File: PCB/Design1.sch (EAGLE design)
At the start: 38 parts, among them J1 FTDI_DEVICE, U1 ATMEGA2560AU

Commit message: meh
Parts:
- added R10: 1MΩ, SparkFun-Resistors:RESISTOR1206
- added Y1: 16MHZ, SparkFun-FreqCtrl:RESONATOR16MHZ
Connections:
- net N$8 renamed VIN_RECTIFIED
- new net XTAL1: R10.1, U1.XTAL1, Y1.3
- new net XTAL2: R10.2, U1.XTAL2, Y1.1
- net GND: now also Y1.2
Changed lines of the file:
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@@
 <part name="U3" library="SparkFun-PowerIC" deviceset="V_REG_LM1117" device="SOT223"/>
 <part name="C7" library="SparkFun-Capacitors" deviceset="CAP_POL" device="PTH1" value="470uF"/>
+<part name="Y1" library="SparkFun-FreqCtrl" deviceset="RESONATOR" device="16MHZ" value="16MHZ"/>
+<part name="R10" library="SparkFun-Resistors" deviceset="RESISTOR" device="1206" value="1MΩ"/>
+<part name="GND8" library="SparkFun-Aesthetics" deviceset="GND" device=""/>
 </parts>
 <sheets>
@@
 <instance part="POWER" gate="G$1" x="5.08" y="33.02"/>
 <instance part="SERIAL" gate="G$1" x="256.54" y="73.66"/>
-<instance part="SUPPLY1" gate="G$1" x="60.96" y="205.74"/>
+<instance part="SUPPLY1" gate="G$1" x="60.96" y="200.66"/>
 <instance part="SUPPLY3" gate="G$1" x="238.76" y="25.4"/>
 <instance part="SUPPLY5" gate="G$1" x="111.76" y="43.18"/>
@@
 <instance part="U3" gate="G$1" x="63.5" y="20.32" rot="MR180"/>
 <instance part="C7" gate="G$1" x="81.28" y="35.56"/>
+<instance part="Y1" gate="G$1" x="53.34" y="210.82" rot="R270"/>
+<instance part="R10" gate="G$1" x="33.02" y="210.82" rot="R90"/>
+<instance part="GND8" gate="1" x="40.64" y="208.28"/>
 </instances>
 <busses>
@@
 <junction x="274.32" y="177.8"/>
 </segment>
+<segment>
+<pinref part="Y1" gate="G$1" pin="2"/>
+<wire x1="45.72" y1="210.82" x2="40.64" y2="210.82" width="0.1524" layer="91"/>
+<pinref part="GND8" gate="1" pin="GND"/>
+</segment>
 </net>
 <net name="RESET" class="0">
@@
 <pinref part="U1" gate="1" pin="RESET"/>
 <wire x1="71.12" y1="218.44" x2="60.96" y2="218.44" width="0.1524" layer="91"/>
-<label x="68.58" y="220.98" size="1.778" layer="95" rot="R180"/>
+<label x="60.96" y="218.44" size="1.778" layer="95"/>
 </segment>
 </net>
@@
 <pinref part="U1" gate="1" pin="(OC0A/OC1C/PCINT7)PB7"/>
 <wire x1="142.24" y1="195.58" x2="152.4" y2="195.58" width="0.1524" layer="91"/>
-<label x="144.78" y="195.58" size="1.27" layer="95"/>
+<label x="144.78" y="195.58" size="1.778" layer="95"/>
 </segment>
 </net>
@@
 <wire x1="71.12" y1="200.66" x2="60.96" y2="200.66" width="0.1524" layer="91"/>
 <pinref part="SUPPLY1" gate="G$1" pin="5V"/>
-<wire x1="60.96" y1="205.74" x2="60.96" y2="200.66" width="0.1524" layer="91"/>
 <junction x="60.96" y="200.66"/>
 </segment>
@@
 </segment>
 </net>
-<net name="N$8" class="0">
+<net name="VIN_RECTIFIED" class="0">
 <segment>
 <pinref part="D2" gate="G$1" pin="C"/>
@@
 </segment>
 </net>
+<net name="XTAL2" class="0">
+<segment>
+<pinref part="Y1" gate="G$1" pin="1"/>
+<pinref part="U1" gate="1" pin="XTAL2"/>
+<wire x1="71.12" y1="213.36" x2="53.34" y2="213.36" width="0.1524" layer="91"/>
+<wire x1="53.34" y1="213.36" x2="53.34" y2="218.44" width="0.1524" layer="91"/>
+<junction x="53.34" y="213.36"/>
+<pinref part="R10" gate="G$1" pin="2"/>
+<wire x1="53.34" y1="218.44" x2="33.02" y2="218.44" width="0.1524" layer="91"/>
+<wire x1="33.02" y1="218.44" x2="33.02" y2="215.9" width="0.1524" layer="91"/>
+</segment>
+</net>
+<net name="XTAL1" class="0">
+<segment>
+<pinref part="Y1" gate="G$1" pin="3"/>
+<pinref part="U1" gate="1" pin="XTAL1"/>
+<wire x1="71.12" y1="208.28" x2="53.34" y2="208.28" width="0.1524" layer="91"/>
+<wire x1="53.34" y1="208.28" x2="53.34" y2="203.2" width="0.1524" layer="91"/>
+<junction x="53.34" y="208.28"/>
+<pinref part="R10" gate="G$1" pin="1"/>
+<wire x1="53.34" y1="203.2" x2="33.02" y2="203.2" width="0.1524" layer="91"/>
+<wire x1="33.02" y1="203.2" x2="33.02" y2="205.74" width="0.1524" layer="91"/>
+</segment>
+</net>

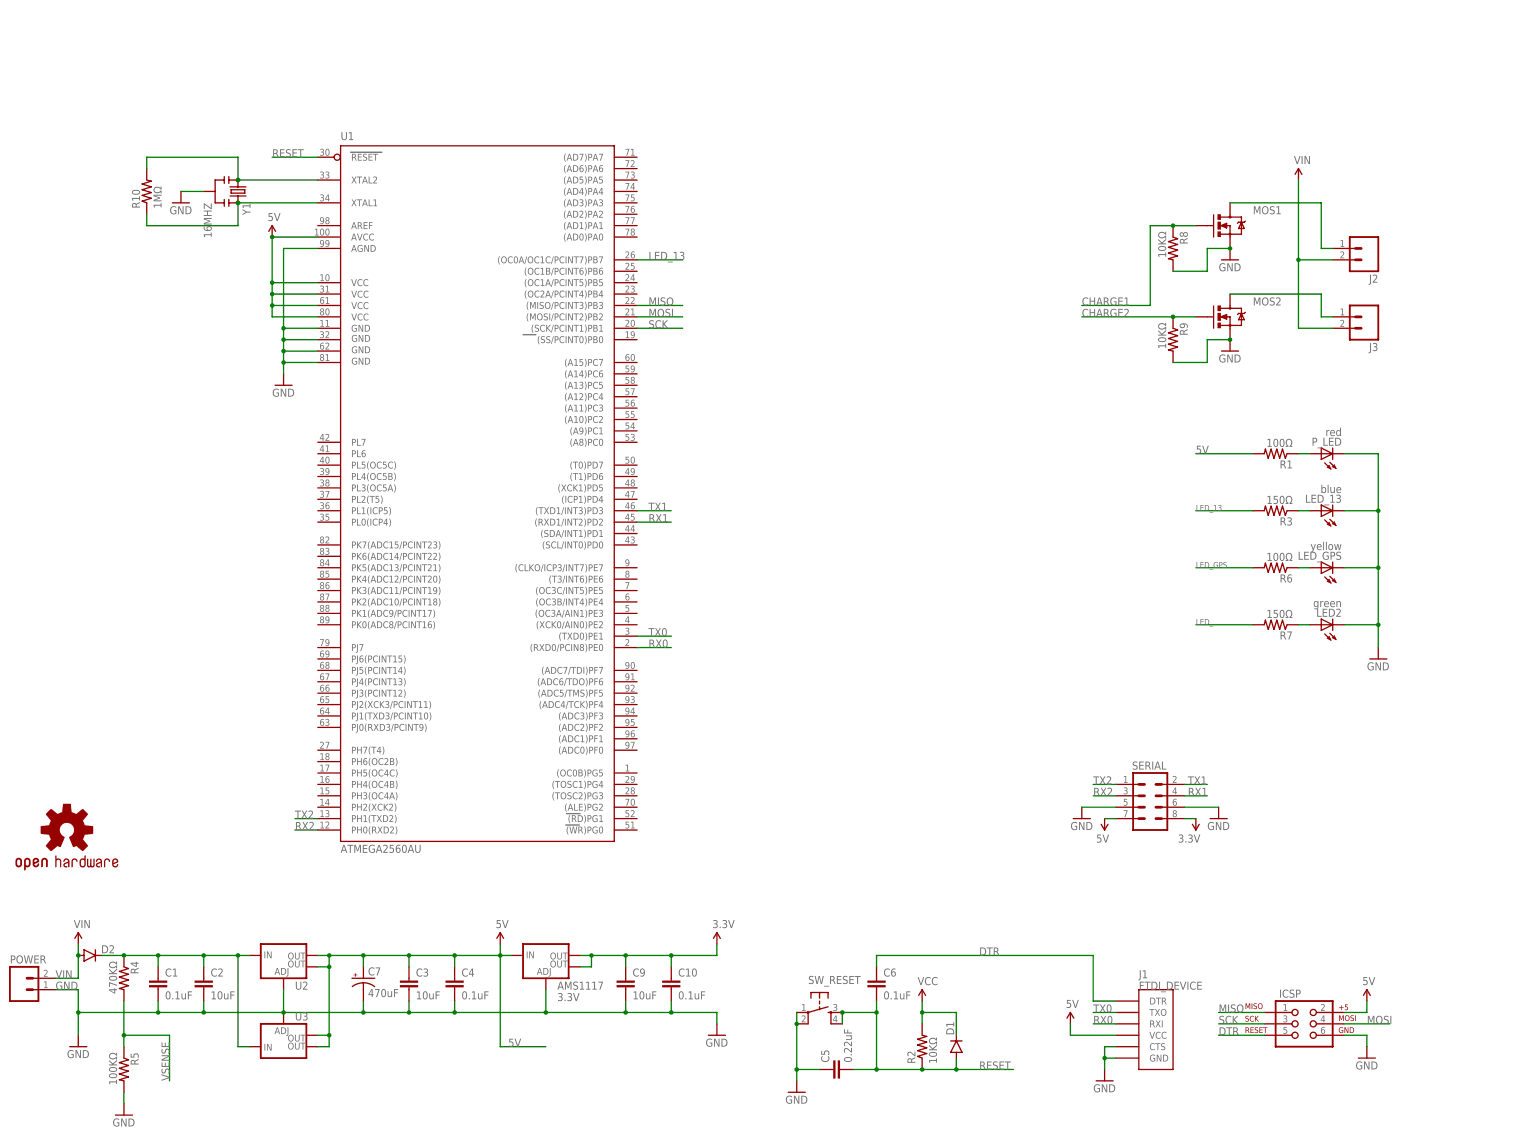
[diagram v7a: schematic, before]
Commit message: Remove 3.3v; clean up Ground near MOSFETS
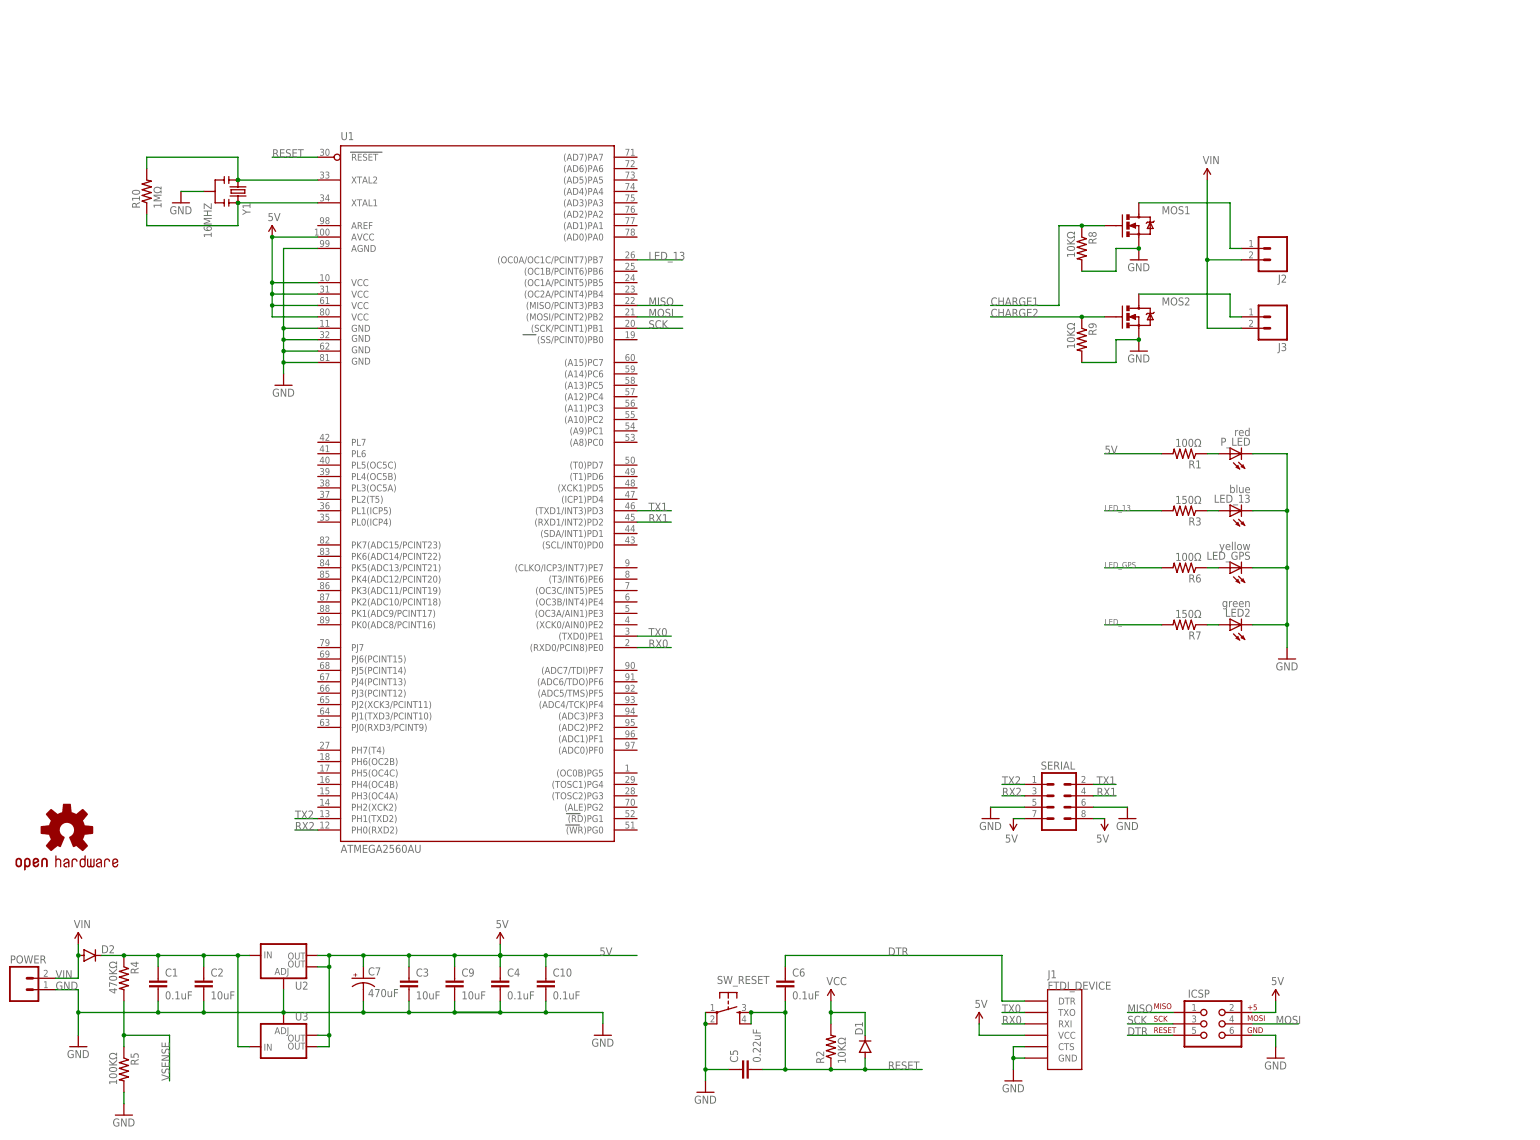
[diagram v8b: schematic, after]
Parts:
- removed AMS1117: 3.3V, SparkFun-PowerIC:V_REG_LM1117SOT223
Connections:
- removed net 3.3V: AMS1117.OUT, AMS1117.OUT@1, C10.1, C9.1, SERIAL.8
- net 5V: now also C10.1, C9.1, SERIAL.8; no longer AMS1117.IN
- net GND: no longer AMS1117.ADJ
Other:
- moved on the sheet: C10, C4, C5, C6, C9, D1, ICSP, J1, J2, J3, LED2, LED_13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
